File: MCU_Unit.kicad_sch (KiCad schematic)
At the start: 1 part, among them U401 STM32WB5MMG

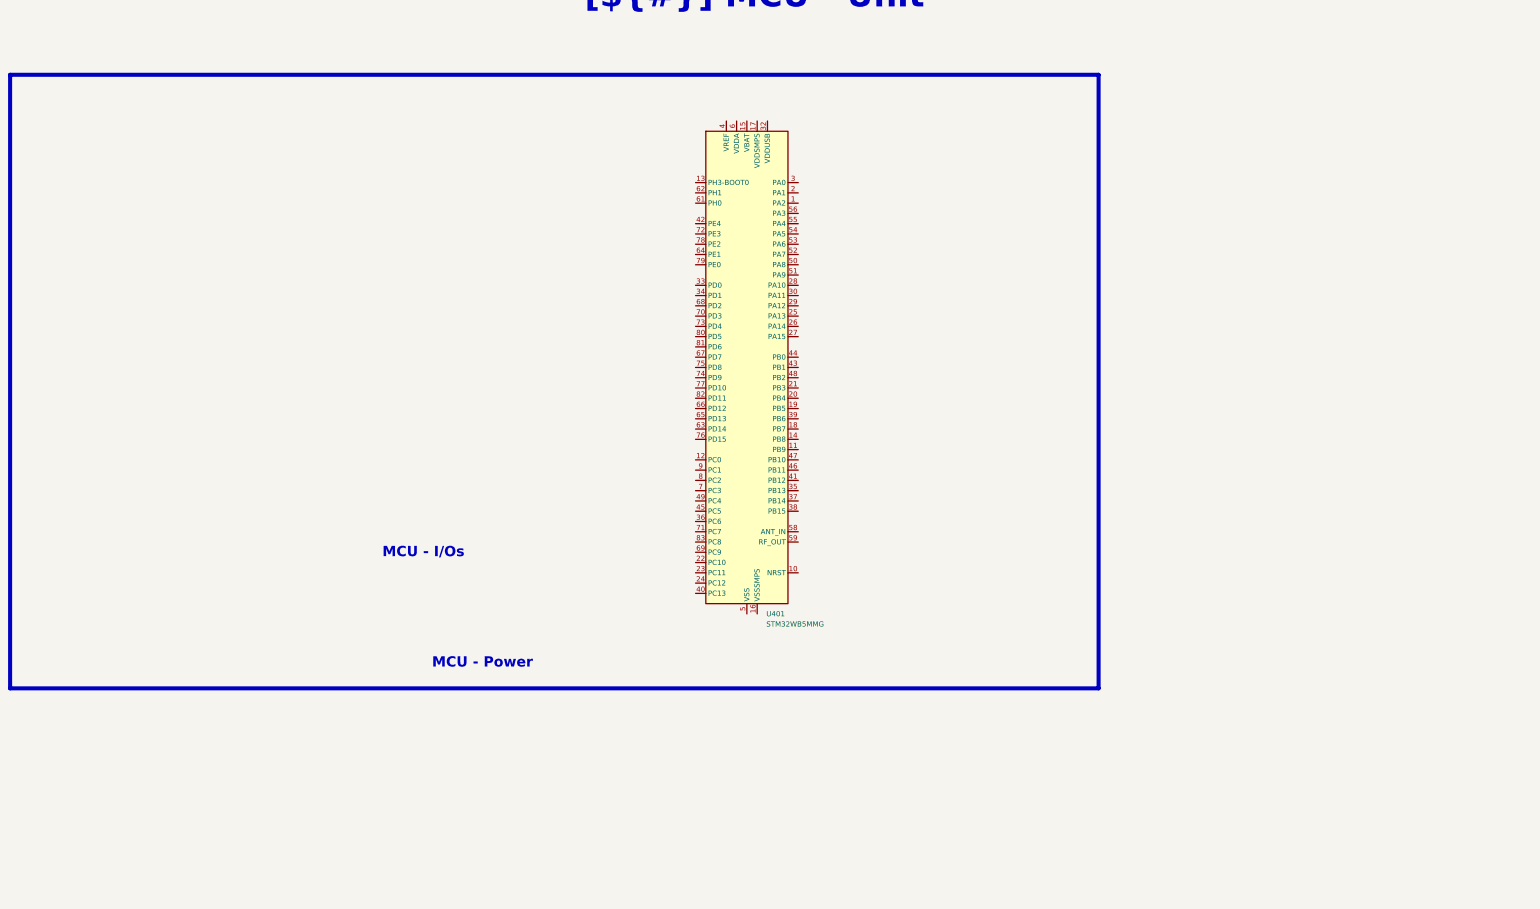
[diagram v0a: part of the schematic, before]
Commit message: Added footprints, images, almost finished all èages except for the MCU
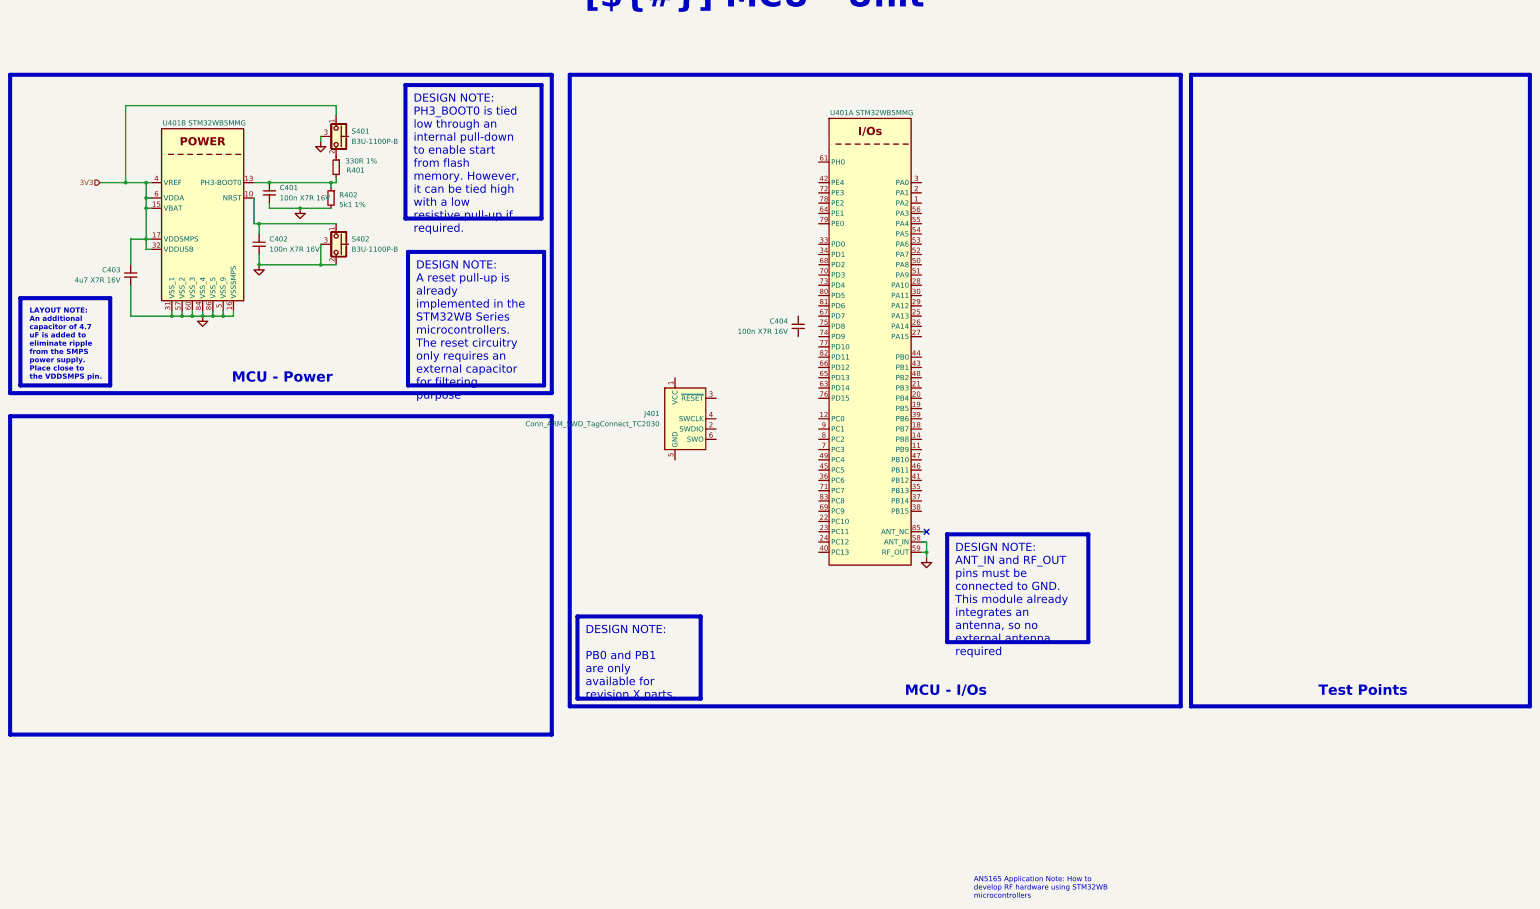
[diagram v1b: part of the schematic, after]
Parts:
- removed U401: STM32WB5MMG, RF_Module:ST-SiP-LGA-86-11x7.3mm, symbol RF_Module:STM32WB5MMG
- added C401, C402, C404: 100n X7R 16V, Capacitor_SMD:C_0402_1005Metric, symbol Device:C_Small
- added C403: 4u7 X7R 16V, Capacitor_SMD:C_0603_1608Metric, symbol Device:C_Small
- added J401: Conn_ARM_SWD_TagConnect_TC2030, Connector:Tag-Connect_TC2030-IDC-FP_2x03_P1.27mm_Vertical, symbol Connector:Conn_ARM_SWD_TagConnect_TC2030
- added R401: 330R 1%, Resistor_SMD:R_0402_1005Metric, symbol Device:R_Small
- added R402: 5k1 1%, Resistor_SMD:R_0402_1005Metric, symbol Device:R_Small
- added S401, S402: B3U-1100P-B, Charge_Manager_FP:B3U1100PB, symbol Charge_Manager_SYM:B3U-1100P
- added U401: STM32WB5MMG, RF_Module:ST-SiP-LGA-86-11x7.3mm, symbol 0_Plume:STM32WB5MMG
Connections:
- new net: R401.1, S401.2
- new net: C401.1, R401.2, R402.1, U401.13 (PH3-BOOT0)
- new net: C402.1, S402.1, U401.10 (NRST)
- new net: U401.31 (VSS), U401.57 (VSS), U401.60 (VSS), U401.84 (VSS), U401.86 (VSS)
- new net 3V3: C403.1, S401.1, U401.15 (VBAT), U401.17 (VDDSMPS), U401.32 (VDDUSB), U401.4 (VREF), U401.6 (VDDA)
- new net GND: C401.2, C402.2, C403.2, R402.2, S401.3, S402.2, S402.3, U401.16 (VSSSMPS), U401.31 (VSS), U401.5 (VSS_9), U401.57 (VSS), U401.58 (ANT_IN), U401.59 (RF_OUT), U401.60 (VSS), U401.84 (VSS), U401.86 (VSS)
- no-connect marks 0 -> 1
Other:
- note added: "AN5165 Application Note: How to develop RF hardware using STM32WB microcontrollers"

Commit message: Added RGB LED, added motor connectors, added test points, imported all 3D models
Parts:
- removed J401: Conn_ARM_SWD_TagConnect_TC2030, Connector:Tag-Connect_TC2030-IDC-FP_2x03_P1.27mm_Vertical, symbol Connector:Conn_ARM_SWD_TagConnect_TC2030
- added J401: Conn_ARM_SWD_TagConnect_TC2030-NL, Connector:Tag-Connect_TC2030-IDC-NL_2x03_P1.27mm_Vertical, symbol Connector:Conn_ARM_SWD_TagConnect_TC2030-NL
- S401, S402: footprint Charge_Manager_FP:B3U1100PB -> 0_Plume:B3U1100PB
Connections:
- new net: U401.31 (VSS), U401.57 (VSS), U401.60 (VSS), U401.84 (VSS), U401.86 (VSS)
- no-connect marks 1 -> 2

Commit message: Finished schematic, imported all footprints, all 3D models and created STM32 project, now need to proofread shematic before layout
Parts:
- removed C404: 100n X7R 16V, Capacitor_SMD:C_0402_1005Metric, symbol Device:C_Small
- removed S401, S402: B3U-1100P-B, 0_Plume:B3U1100PB, symbol Charge_Manager_SYM:B3U-1100P
- added D401: ESDS314, Package_TO_SOT_SMD:SOT-23-5, symbol 0_Plume:ESDS314
- added J401: Solder Holes 4x1 2.54mm 22AWG, Connector_PinHeader_2.54mm:PinHeader_1x04_P2.54mm_Vertical, symbol Connector_Generic:Conn_01x04
- added J403, J404: Solder Wire Pad 2x4mm, 0_Plume:SolderWirePad_SMD_2x4mm, symbol Connector_Generic:Conn_01x01
- added R403, R404: 22R 1%, Resistor_SMD:R_0402_1005Metric, symbol Device:R_Small
- added SW401, SW402, SW404, SW405, SW406, SW407: KMR232NG ULC, 0_Plume:KMR232NGULCLFS, symbol 0_Plume:KMR2_series
- added SW403: CAS-D20A1, 0_Plume:CAS-D2xx, symbol 0_Plume:CAS-D20A1
- added TP401: BUTTON1, 0_Plume:TestPoint_Pad_D0.5mm_Back, symbol Connector:TestPoint
- added TP402: BUTTON2, 0_Plume:TestPoint_Pad_D0.5mm_Back, symbol Connector:TestPoint
- added TP403: BUTTON3, 0_Plume:TestPoint_Pad_D0.5mm_Back, symbol Connector:TestPoint
- added TP404: BUTTON4, 0_Plume:TestPoint_Pad_D0.5mm_Back, symbol Connector:TestPoint
- added TP405: SWITCH1, 0_Plume:TestPoint_Pad_D0.5mm_Back, symbol Connector:TestPoint
- added TP406: SWITCH2, 0_Plume:TestPoint_Pad_D0.5mm_Back, symbol Connector:TestPoint
- J402: renamed from J401; symbol Connector:Conn_ARM_SWD_TagConnect_TC2030-NL -> 0_Plume:Conn_ARM_SWD_TagConnect_TC2030_NL
- U401: value STM32WB5MMG -> STM32WB5MMGH6TR; Manufacturer (none) -> STMicroelectronics; Manufacturer Part Number (none) -> STM32WB5MMGH6TR; Supplier (none) -> Mouser Electronics; Supplier Part Number (none) -> 511-STM32WB5MMGH6TR
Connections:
- net 3V3: now also SW401.2, SW401.3
- net GND: now also J402.5 (GND), D401.2 (GND), J401.1 (Pin_1), SW402.1, SW402.4, SW403.3, SW403.6, SW404.1, SW404.4, SW405.1, SW405.4, SW406.1, SW406.4, SW407.1, SW407.4
- net +3V3: now reaches J402.1 (VCC)
- net +3V3: now also D401.5 (I/O4), J401.4 (Pin_4), SW403.1, SW403.4
- net SWDIO: now reaches J402.2 (SWDIO)
- net SWDIO: now also U401.25 (PA13)
- net ~{RESET}: now reaches J402.3 (~{RESET})
- net ~{RESET}: now also C402.1, U401.10 (NRST), SW402.2, SW402.3
- net SWCLK: now reaches J402.4 (SWCLK)
- net SWCLK: now also U401.26 (PA14)
- net SWO: now reaches J402.6 (SWO)
- net SWO: now also U401.21 (PB3)
- net at R401.1: now also SW401.1, SW401.4
- net BOOT0: now reaches C401.1, R401.2, R402.1, U401.13 (PH3-BOOT0)
- net I2C1_SDA: now reaches U401.11 (PB9)
- net I2C3_SCL: now reaches U401.12 (PC0)
- net I2C3_SCL: now also J403.1 (Pin_1)
- net I2C1_SCL: now reaches U401.14 (PB8)
- net at U401.28 (PA10): now also R404.1
- net nFAULT17: now reaches U401.33 (PD0)
- net nFAULT16: now reaches U401.34 (PD1)
- net nFAULT15: now reaches U401.35 (PB13)
- net nFAULT14: now reaches U401.36 (PC6)
- net nFAULT13: now reaches U401.37 (PB14)
- net nFAULT12: now reaches U401.38 (PB15)
- net nFAULT11: now reaches U401.39 (PB6)
- net nFAULT10: now reaches U401.40 (PC13)
- net nFAULT9: now reaches U401.41 (PB12)
- net nFAULT8: now reaches U401.42 (PE4)
- net nFAULT7: now reaches U401.43 (PB1)
- net nFAULT6: now reaches U401.44 (PB0)
- net nFAULT5: now reaches U401.45 (PC5)
- net nFAULT4: now reaches U401.46 (PB11)
- net nFAULT3: now reaches U401.47 (PB10)
- net nFAULT2: now reaches U401.48 (PB2)
- net nFAULT1: now reaches U401.49 (PC4)
- net nFAULT0: now reaches U401.50 (PA8)
- net at U401.51 (PA9): now also R403.1
- net I2C3_SDA: now reaches U401.9 (PC1)
- net I2C3_SDA: now also J404.1 (Pin_1)
- new net: U401.31 (VSS), U401.57 (VSS), U401.60 (VSS), U401.84 (VSS), U401.86 (VSS)
- new net BUTTON1: SW404.2, SW404.3, TP401.1
- new net BUTTON2: SW405.2, SW405.3, TP402.1
- new net BUTTON3: SW406.2, SW406.3, TP403.1
- new net BUTTON4: SW407.2, SW407.3, TP404.1
- new net SWITCH1: SW403.5, TP405.1
- new net SWITCH2: SW403.2, TP406.1
- new net USART1_RX: D401.3 (I/O2), J401.3 (Pin_3), R404.2
- new net USART1_TX: D401.1 (I/O1), J401.2 (Pin_2), R403.2
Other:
- note added: "AN2606 Application Note: STM32 microcontroller system memory boot mode"
- moved on the sheet: J402, R401, R402

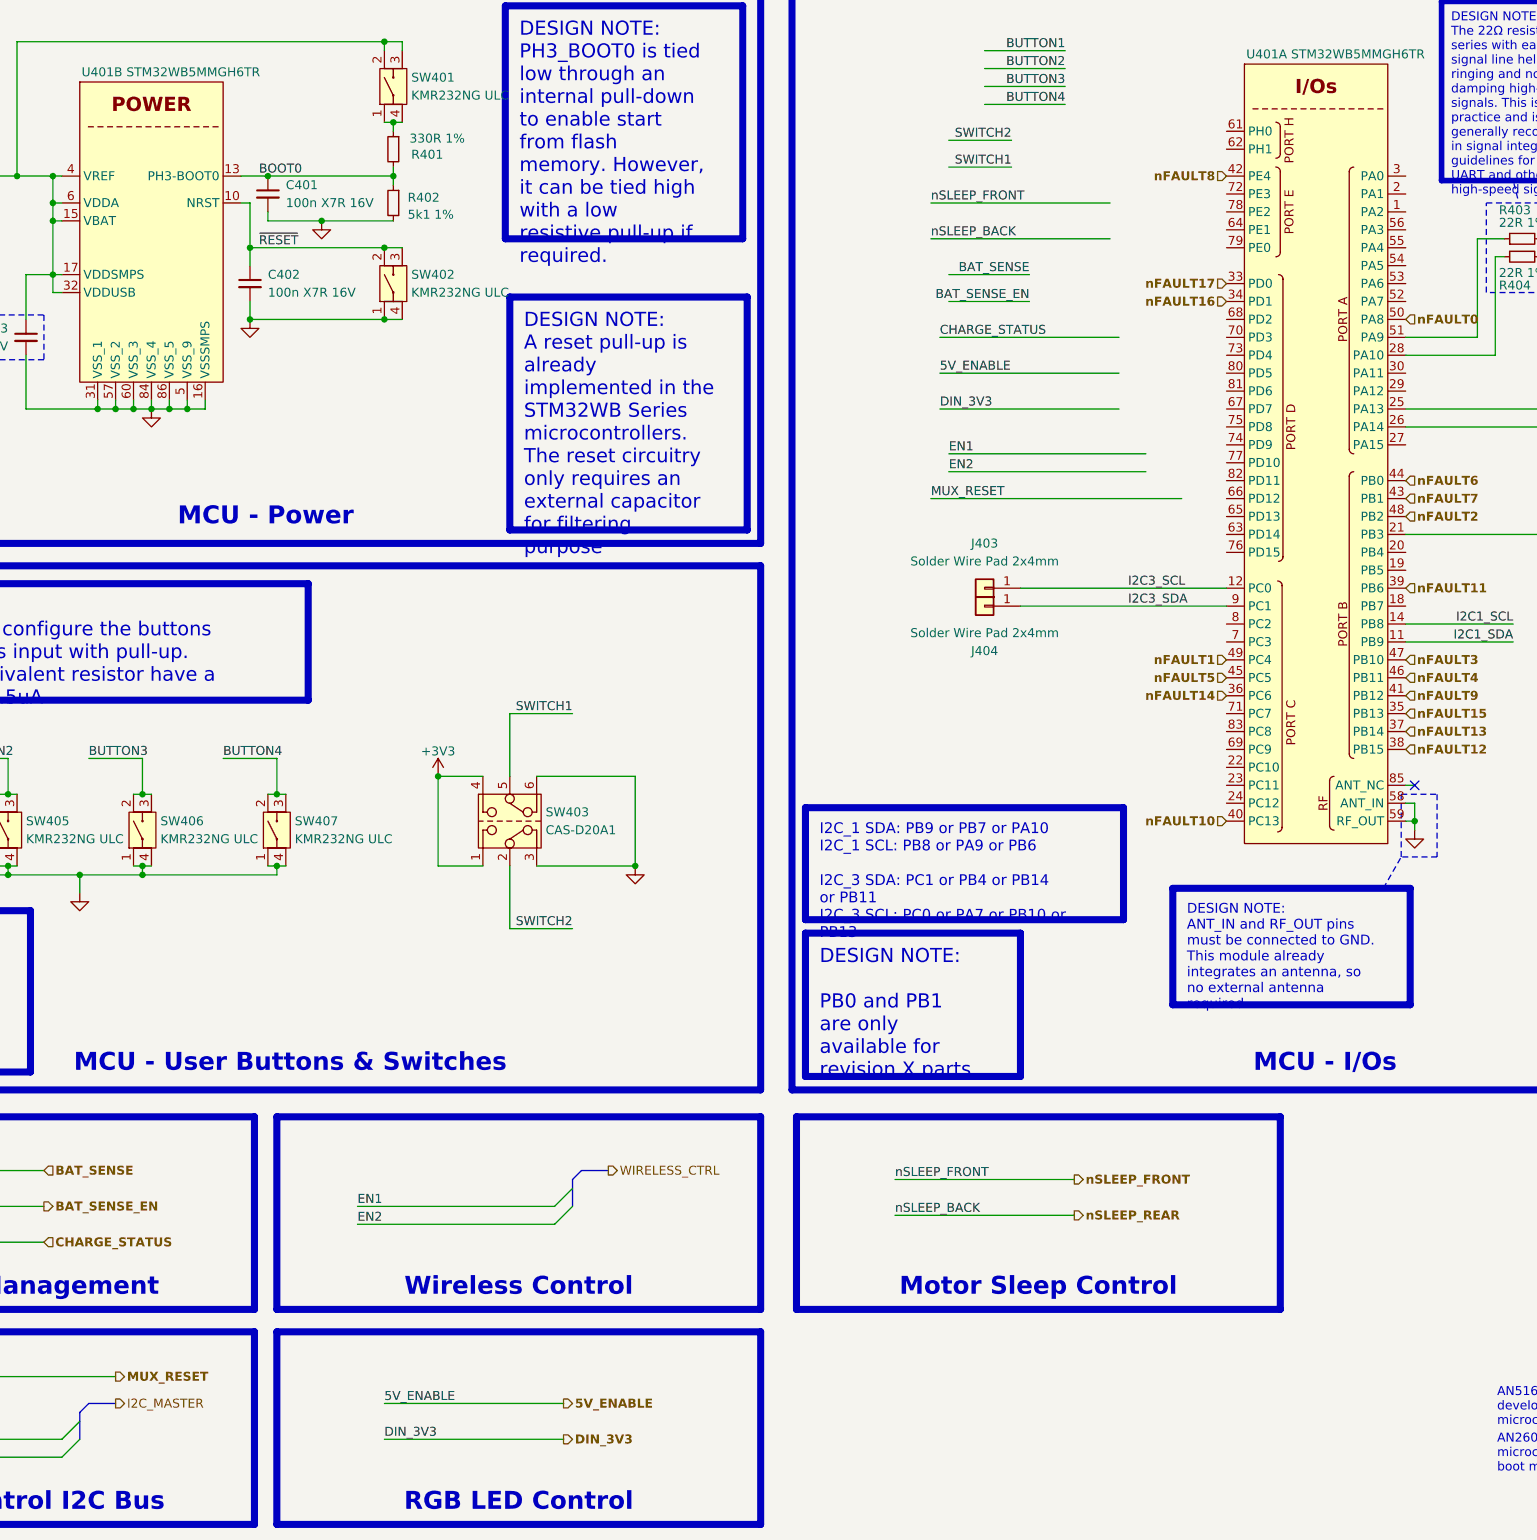
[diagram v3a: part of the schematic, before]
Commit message: Reviewed shematic, cleaned all DRC errors, chosed stackup, started layout
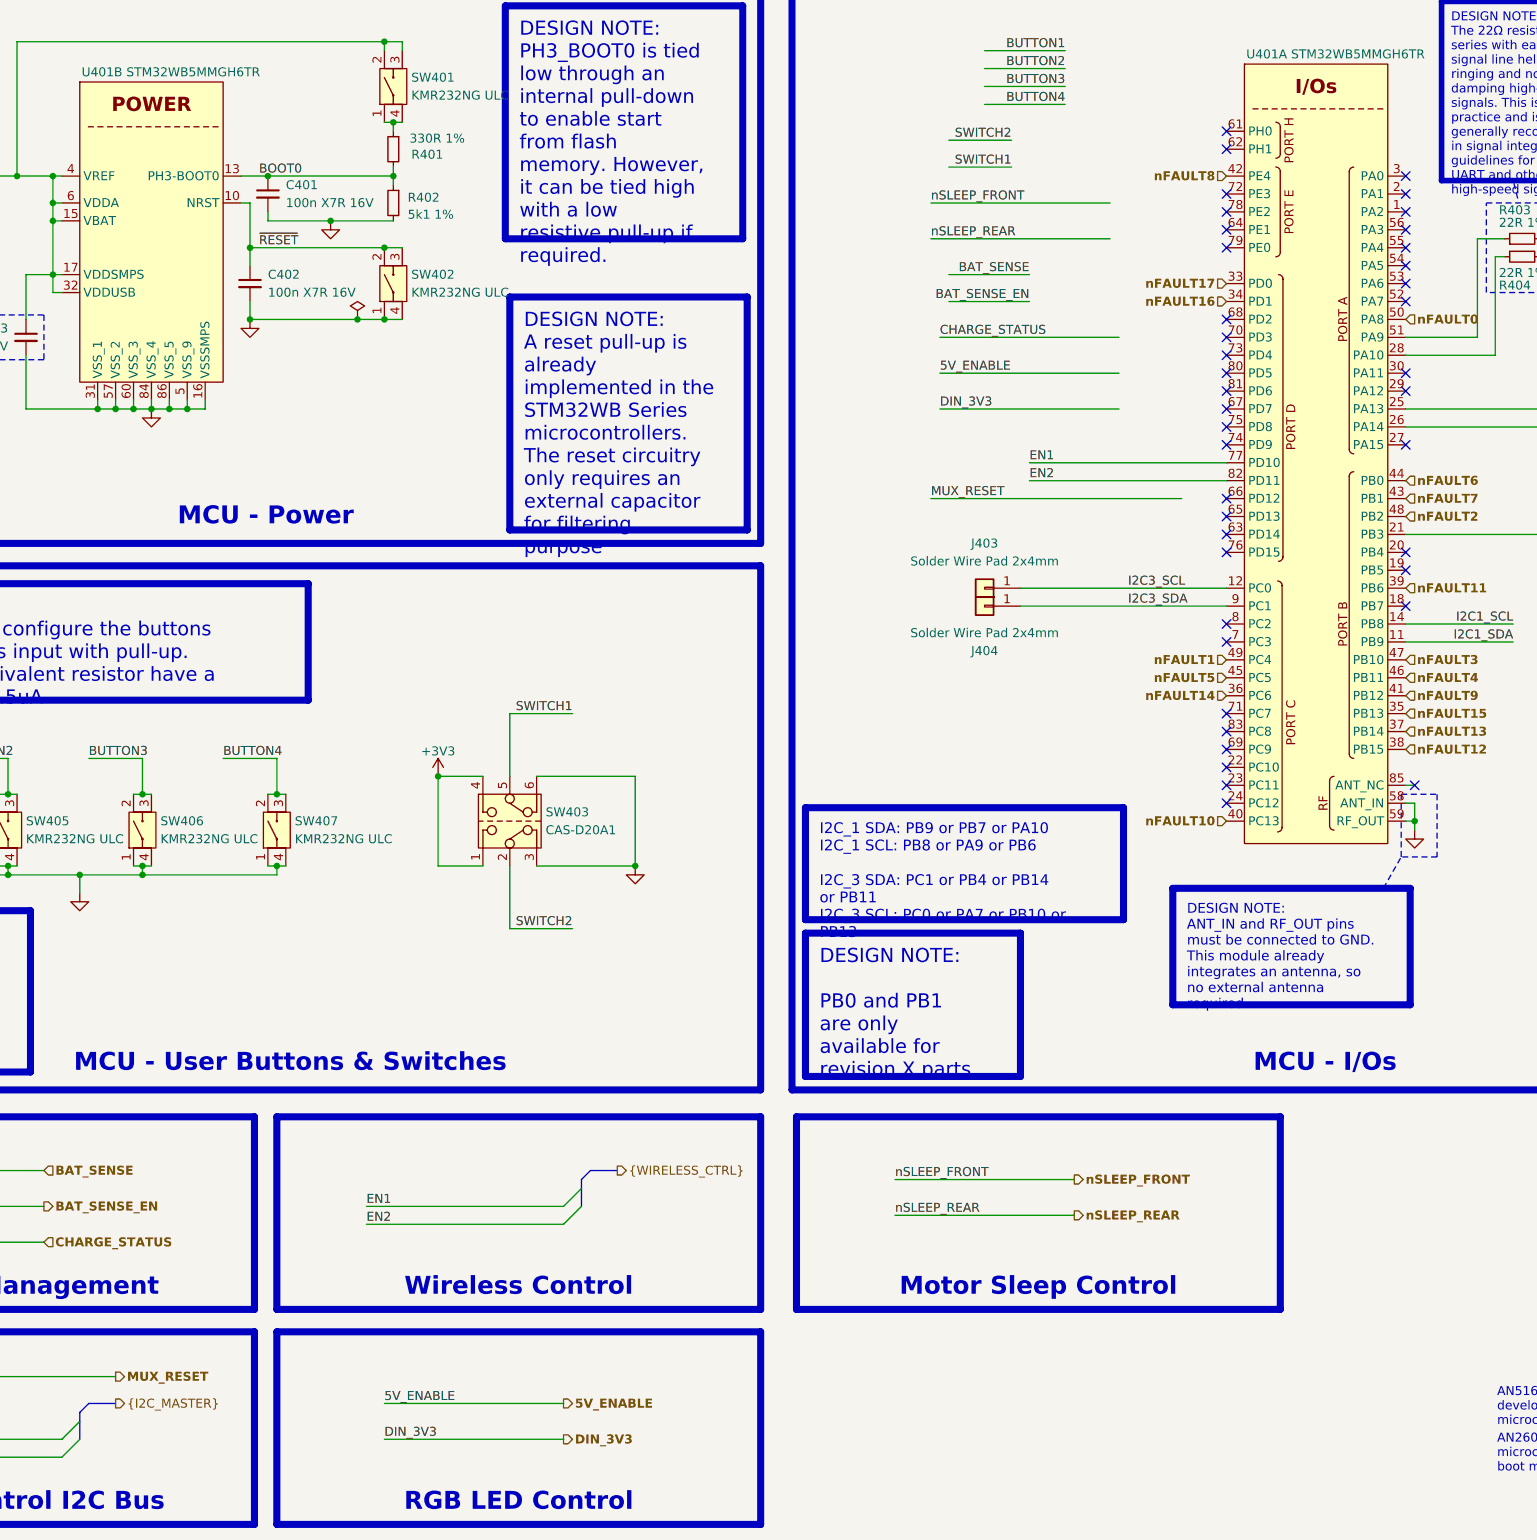
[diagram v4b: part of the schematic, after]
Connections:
- net EN1: now also U401.77 (PD10)
- net EN2: now also U401.82 (PD11)
- no-connect marks 2 -> 42

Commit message: Cleaned repo, cleaned and exported shematic, advanced rough layout
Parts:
- removed R402: 5k1 1%, Resistor_SMD:R_0402_1005Metric, symbol Device:R_Small
- added C404, C405, C406, C407: 100n X7R 16V, Capacitor_SMD:C_0402_1005Metric, symbol Device:C_Small
- added R609: 10k 1%, Resistor_SMD:R_0402_1005Metric, symbol Device:R_Small
- J403, J404: value Solder Wire Pad 2x4mm -> Solder Wire Pad 1,5x3mm; footprint 0_Plume:SolderWirePad_SMD_2x4mm -> 0_Plume:SolderWirePad_SMD_1,5x3mm
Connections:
- net BOOT0: now also R609.2
- net BUTTON1: now also C404.1
- net BUTTON2: now also C405.1
- net BUTTON3: now also C406.1
- net BUTTON4: now also C407.1
- net GND: now also C404.2, C405.2, C406.2, C407.2, R609.1
- net USART1_RX: now also D401.1 (I/O1); no longer D401.3 (I/O2)
- net USART1_TX: now also D401.3 (I/O2); no longer D401.1 (I/O1)
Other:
- note added: "Debounce a Switch - Texas Instrument"
- moved on the sheet: SW401, SW403, SW404, SW405, SW406, SW407, TP401, TP402, TP403, TP404, TP405, TP406
